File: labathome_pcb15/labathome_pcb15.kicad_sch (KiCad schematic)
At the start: 40 parts, among them J11 USB_ESP32, J15 CAN RS 485, J17 Micro_SD_Card_Det1, J21 GPIO, J22 Volts, J6 I2C, J7 PROG, SW2 YELLOW, SW3 GREEN, SW3 Reset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

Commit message: Updates in PCB, arduino test firmware
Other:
- note added: "Display (ST7789, 1,3'')"
- note added: "I2C addresses (0-127): AHT20: 0x38 BH1750 0x23 BMPx80: 0x76 CCS811: 0x5A LSM6DS3: 0x6A NAU88C22: 0x1A SCD41: 0x62 TCS34725: 0x29"
- note removed: "Display"
- note removed: "I2C addresses (0-127): AHT20: 0x38 BH1750 0x23 BMPx80: 0x76 CCS811: 0x5A LSM6DS3: 0x6A NAU88C22: 0x1A SCD41 0x62 TCS34725 0x29"
- company: (none) -> Klaus Liebler
- title: (none) -> lab@home
- moved on the sheet: C53, R39, R40, R41, SW3, SW4

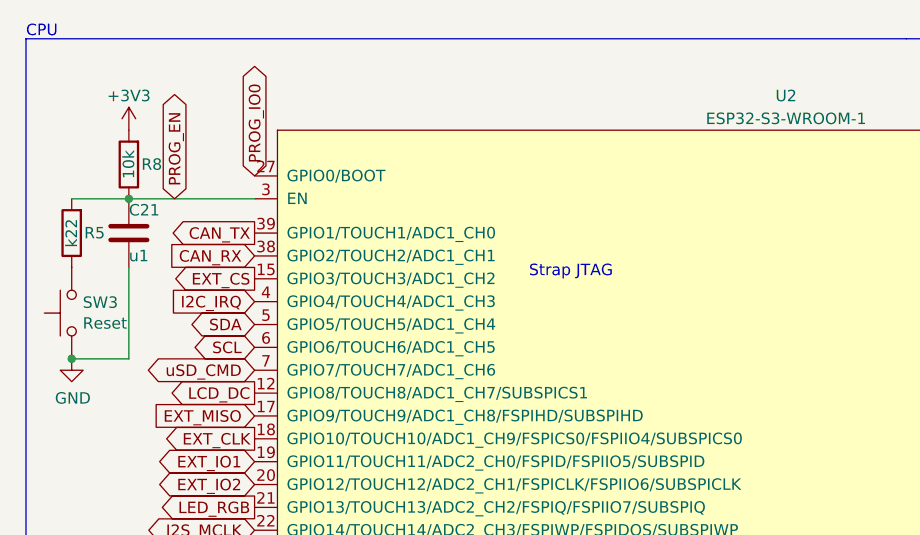
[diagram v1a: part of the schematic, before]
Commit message: Reverse mount LEDs, switch
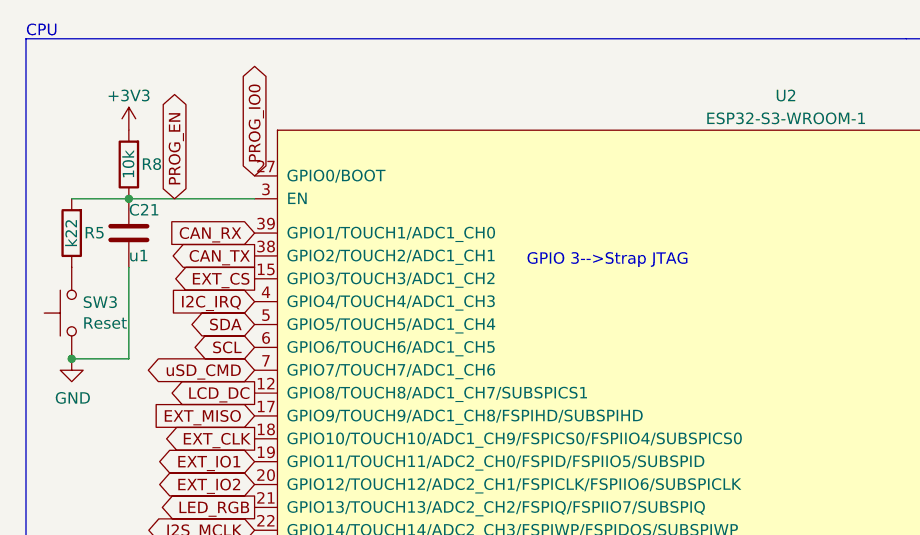
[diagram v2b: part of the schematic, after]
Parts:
- SW3: footprint liebler_MECH:SW_SPST_TL3342_smaller_handsolder -> liebler_MECH:Button_2x4x3,5_handsolder
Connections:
- net CAN_RX: now also U2.39 (GPIO1/TOUCH1/ADC1_CH0); no longer U2.38 (GPIO2/TOUCH2/ADC1_CH1)
- net CAN_TX: now also U2.38 (GPIO2/TOUCH2/ADC1_CH1); no longer U2.39 (GPIO1/TOUCH1/ADC1_CH0)
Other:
- note added: "GPIO 3-->Strap JTAG"
- note removed: "Strap JTAG"
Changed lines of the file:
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@@
 		)
 	)
-	(text "Strap JTAG"
+	(text "GPIO 3-->Strap JTAG"
 		(exclude_from_sim no)
-		(at 68.58 40.64 0)
+		(at 68.326 39.37 0)
 		(effects
 			(font
@@
 	(global_label "CAN_TX"
 		(shape output)
-		(at 38.1 35.56 180)
-		(fields_autoplaced yes)
-		(effects
-			(font
-				(size 1.27 1.27)
-			)
-			(justify right)
-		)
-		(property "Intersheetrefs" "${INTERSHEET_REFS}"
-			(at 28.281 35.56 0)
+		(at 38.1 38.1 180)
+		(fields_autoplaced yes)
+		(effects
+			(font
+				(size 1.27 1.27)
+			)
+			(justify right)
+		)
+		(property "Intersheetrefs" "${INTERSHEET_REFS}"
+			(at 28.281 38.1 0)
 			(effects
 				(font
@@
 	(global_label "CAN_RX"
 		(shape input)
-		(at 38.1 38.1 180)
-		(fields_autoplaced yes)
-		(effects
-			(font
-				(size 1.27 1.27)
-			)
-			(justify right)
-		)
-		(property "Intersheetrefs" "${INTERSHEET_REFS}"
-			(at 27.9786 38.1 0)
+		(at 38.1 35.56 180)
+		(fields_autoplaced yes)
+		(effects
+			(font
+				(size 1.27 1.27)
+			)
+			(justify right)
+		)
+		(property "Intersheetrefs" "${INTERSHEET_REFS}"
+			(at 27.9786 35.56 0)
 			(effects
 				(font
@@
 			)
 		)
-		(property "Footprint" "liebler_MECH:SW_SPST_TL3342_smaller_handsolder"
+		(property "Footprint" "liebler_MECH:Button_2x4x3,5_handsolder"
 			(at 12.7 44.45 0)
 			(effects

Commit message: Various last minute
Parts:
- C21, C26, C27, C32, C40, C53: footprint Capacitor_SMD:C_0402_1005Metric -> Capacitor_SMD:C_0201_0603Metric
- J7: value PROG -> PROG ESP
- R17, R44: value 1k -> 10k; footprint Resistor_SMD:R_0402_1005Metric -> Resistor_SMD:R_0201_0603Metric
- R39, R41, R56, R57, R58, R61, R62, R67, R8: footprint Resistor_SMD:R_0402_1005Metric -> Resistor_SMD:R_0201_0603Metric
- R40, R66: value 1k -> k22
- SW3, SW4: footprint Button_Switch_THT:SW_PUSH-12mm -> liebler_MECH:SW_Push_1P1T_NO_6x6mm_H6.5mm_Reverse
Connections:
- net GND: no longer SW2.MP
- new net GNDA: SW2.MP
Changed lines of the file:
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@@
 	)
 	(junction
-		(at 101.6 123.19)
-		(diameter 0)
-		(color 0 0 0 0)
-	)
-	(junction
 		(at 16.51 82.55)
 		(diameter 0)
@@
 	)
 	(junction
-		(at 203.2 38.1)
+		(at 101.6 123.19)
 		(diameter 0)
 		(color 0 0 0 0)
 	)
 	(junction
-		(at 208.28 41.91)
+		(at 203.2 38.1)
 		(diameter 0)
 		(color 0 0 0 0)
 	)
 	(junction
-		(at 142.24 105.41)
+		(at 208.28 41.91)
 		(diameter 0)
 		(color 0 0 0 0)
 	)
 	(junction
-		(at 100.33 123.19)
+		(at 142.24 105.41)
 		(diameter 0)
 		(color 0 0 0 0)
@@
 		)
 	)
-	(wire
-		(pts
-			(xy 92.71 123.19) (xy 100.33 123.19)
-		)
-		(stroke
-			(width 0)
-			(type default)
-		)
-	)
 	(polyline
 		(pts
@@
 		)
 	)
-	(wire
-		(pts
-			(xy 100.33 123.19) (xy 101.6 123.19)
-		)
-		(stroke
-			(width 0)
-			(type default)
-		)
-	)
 	(rectangle
 		(start 176.53 77.47)
@@
 	)
 	(symbol
+		(lib_id "power:GNDA")
+		(at 92.71 123.19 0)
+		(unit 1)
+		(exclude_from_sim no)
+		(in_bom yes)
+		(on_board yes)
+		(dnp no)
+		(fields_autoplaced yes)
+		(property "Reference" "#PWR0125"
+			(at 92.71 129.54 0)
+			(effects
+				(font
+					(size 1.27 1.27)
+				)
+				(hide yes)
+			)
+		)
+		(property "Value" "GNDA"
+			(at 92.71 128.27 0)
+			(effects
+				(font
+					(size 1.27 1.27)
+				)
+			)
+		)
+		(property "Footprint" ""
+			(at 92.71 123.19 0)
+			(effects
+				(font
+					(size 1.27 1.27)
+				)
+				(hide yes)
+			)
+		)
+		(property "Datasheet" ""
+			(at 92.71 123.19 0)
+			(effects
+				(font
+					(size 1.27 1.27)
+				)
+				(hide yes)
+			)
+		)
+		(property "Description" "Power symbol creates a global label with name \"GNDA\" , analog ground"
+			(at 92.71 123.19 0)
+			(effects
+				(font
+					(size 1.27 1.27)
+				)
+				(hide yes)
+			)
+		)
+		(pin "1"
+		)
+		(instances
+			(project "labathome_pcb15"
+				(path "/e4d6926a-1a8b-424d-97c4-66b6ad87e4ac"
+					(reference "#PWR0125")
+					(unit 1)
+				)
+			)
+		)
+	)
+	(symbol
 		(lib_id "power:GND")
 		(at 33.02 102.87 90)
@@
 			)
 		)
-		(property "Footprint" "Capacitor_SMD:C_0402_1005Metric"
+		(property "Footprint" "Capacitor_SMD:C_0201_0603Metric"
 			(at 150.1648 128.27 0)
 			(effects
@@
 			)
 		)
-		(property "Value" "PROG"
+		(property "Value" "PROG ESP"
 			(at 195.58 81.8896 0)
 			(effects
@@
 			)
 		)
-		(property "Footprint" "Resistor_SMD:R_0402_1005Metric"
+		(property "Footprint" "Resistor_SMD:R_0201_0603Metric"
 			(at 17.272 114.3 90)
 			(effects
@@
 			)
 		)
-		(property "Footprint" "Resistor_SMD:R_0402_1005Metric"
+		(property "Footprint" "Resistor_SMD:R_0201_0603Metric"
 			(at 154.432 109.22 90)
 			(effects
@@
 			)
 		)
-		(property "Value" "1k"
+		(property "Value" "10k"
 			(at 85.09 121.92 90)
 			(effects
@@
 			)
 		)
-		(property "Footprint" "Resistor_SMD:R_0402_1005Metric"
+		(property "Footprint" "Resistor_SMD:R_0201_0603Metric"
 			(at 86.868 121.92 90)
 			(effects
@@
 			)
 		)
-		(property "Footprint" "Resistor_SMD:R_0402_1005Metric"
+		(property "Footprint" "Resistor_SMD:R_0201_0603Metric"
 			(at 109.982 144.78 90)
 			(effects
@@
 	)
 	(symbol
-		(lib_id "power:GND")
-		(at 100.33 123.19 0)
-		(unit 1)
-		(exclude_from_sim no)
-		(in_bom yes)
-		(on_board yes)
-		(dnp no)
-		(property "Reference" "#PWR0125"
-			(at 100.33 129.54 0)
-			(effects
-				(font
-					(size 1.27 1.27)
-				)
-				(hide yes)
-			)
-		)
-		(property "Value" "GND"
-			(at 104.394 125.73 0)
-			(effects
-				(font
-					(size 1.27 1.27)
-				)
-			)
-		)
-		(property "Footprint" ""
-			(at 100.33 123.19 0)
-			(effects
-				(font
-					(size 1.27 1.27)
-				)
-				(hide yes)
-			)
-		)
-		(property "Datasheet" ""
-			(at 100.33 123.19 0)
-			(effects
-				(font
-					(size 1.27 1.27)
-				)
-				(hide yes)
-			)
-		)
-		(property "Description" "Power symbol creates a global label with name \"GND\" , ground"
-			(at 100.33 123.19 0)
-			(effects
-				(font
-					(size 1.27 1.27)
-				)
-				(hide yes)
-			)
-		)
-		(pin "1"
-		)
-		(instances
-			(project "labathome_pcb15"
-				(path "/e4d6926a-1a8b-424d-97c4-66b6ad87e4ac"
-					(reference "#PWR0125")
-					(unit 1)
-				)
-			)
-		)
-	)
-	(symbol
 		(lib_id "Device:C")
 		(at 110.49 116.84 180)
@@
 			)
 		)
-		(property "Footprint" "Capacitor_SMD:C_0402_1005Metric"
+		(property "Footprint" "Capacitor_SMD:C_0201_0603Metric"
 			(at 109.5248 113.03 0)
 			(effects
@@
 			)
 		)
-		(property "Footprint" "Capacitor_SMD:C_0402_1005Metric"
+		(property "Footprint" "Capacitor_SMD:C_0201_0603Metric"
 			(at 17.4752 90.17 0)
 			(effects
@@
 			)
 		)
-		(property "Footprint" "Resistor_SMD:R_0402_1005Metric"
+		(property "Footprint" "Resistor_SMD:R_0201_0603Metric"
 			(at 140.462 116.84 90)
 			(effects
@@
 			)
 		)
-		(property "Value" "1k"
+		(property "Value" "k22"
 			(at 105.41 148.59 90)
 			(effects
@@
 			)
 		)
-		(property "Footprint" "Capacitor_SMD:C_0402_1005Metric"
+		(property "Footprint" "Capacitor_SMD:C_0201_0603Metric"
 			(at 110.7948 148.59 0)
 			(effects
@@
 			)
 		)
-		(property "Footprint" "Resistor_SMD:R_0402_1005Metric"
+		(property "Footprint" "Resistor_SMD:R_0201_0603Metric"
 			(at 134.112 121.92 90)
 			(effects
@@
 	)
 	(symbol
+		(lib_id "power:GND")
+		(at 101.6 123.19 0)
+		(unit 1)
+		(exclude_from_sim no)
+		(in_bom yes)
+		(on_board yes)
+		(dnp no)
+		(property "Reference" "#PWR0203"
+			(at 101.6 129.54 0)
+			(effects
+				(font
+					(size 1.27 1.27)
+				)
+				(hide yes)
+			)
+		)
+		(property "Value" "GND"
+			(at 101.6 128.27 90)
+			(effects
+				(font
+					(size 1.27 1.27)
+				)
+			)
+		)
+		(property "Footprint" ""
+			(at 101.6 123.19 0)
+			(effects
+				(font
+					(size 1.27 1.27)
+				)
+				(hide yes)
+			)
+		)
+		(property "Datasheet" ""
+			(at 101.6 123.19 0)
+			(effects
+				(font
+					(size 1.27 1.27)
+				)
+				(hide yes)
+			)
+		)
+		(property "Description" "Power symbol creates a global label with name \"GND\" , ground"
+			(at 101.6 123.19 0)
+			(effects
+				(font
+					(size 1.27 1.27)
+				)
+				(hide yes)
+			)
+		)
+		(pin "1"
+		)
+		(instances
+			(project "labathome_pcb15"
+				(path "/e4d6926a-1a8b-424d-97c4-66b6ad87e4ac"
+					(reference "#PWR0203")
+					(unit 1)
+				)
+			)
+		)
+	)
+	(symbol
 		(lib_id "Device:C")
 		(at 22.86 106.68 180)
@@
 			)
 		)
-		(property "Footprint" "Capacitor_SMD:C_0402_1005Metric"
+		(property "Footprint" "Capacitor_SMD:C_0201_0603Metric"
 			(at 21.8948 102.87 0)
 			(effects
@@
 			)
 		)
-		(property "Footprint" "Resistor_SMD:R_0402_1005Metric"
+		(property "Footprint" "Resistor_SMD:R_0201_0603Metric"
 			(at 79.502 148.59 90)
 			(effects
@@
 			)
 		)
-		(property "Footprint" "Resistor_SMD:R_0402_1005Metric"
+		(property "Footprint" "Resistor_SMD:R_0201_0603Metric"
 			(at 149.352 111.76 90)
 			(effects
@@
 			)
 		)
-		(property "Footprint" "Button_Switch_THT:SW_PUSH-12mm"
+		(property "Footprint" "liebler_MECH:SW_Push_1P1T_NO_6x6mm_H6.5mm_Reverse"
 			(at 96.52 153.67 0)
 			(effects
@@
 			)
 		)
-		(property "Value" "1k"
+		(property "Value" "k22"
 			(at 105.41 113.03 90)
 			(effects
@@
 			)
 		)
-		(property "Footprint" "Resistor_SMD:R_0402_1005Metric"
+		(property "Footprint" "Resistor_SMD:R_0201_0603Metric"
 			(at 25.908 27.94 90)
 			(effects
@@
 			)
 		)
-		(property "Footprint" "Button_Switch_THT:SW_PUSH-12mm"
+		(property "Footprint" "liebler_MECH:SW_Push_1P1T_NO_6x6mm_H6.5mm_Reverse"
 			(at 76.2 139.7 0)
 			(effects
@@
 			)
 		)
-		(property "Footprint" "Capacitor_SMD:C_0402_1005Metric"
+		(property "Footprint" "Capacitor_SMD:C_0201_0603Metric"
 			(at 25.0952 39.37 0)
 			(effects
@@
 			)
 		)
-		(property "Footprint" "Resistor_SMD:R_0402_1005Metric"
+		(property "Footprint" "Resistor_SMD:R_0201_0603Metric"
 			(at 108.712 109.22 90)
 			(effects
@@
 			)
 		)
-		(property "Value" "1k"
+		(property "Value" "10k"
 			(at 85.09 109.22 90)
 			(effects
@@
 			)
 		)
-		(property "Footprint" "Resistor_SMD:R_0402_1005Metric"
+		(property "Footprint" "Resistor_SMD:R_0201_0603Metric"
 			(at 86.868 109.22 90)
 			(effects

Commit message: PCB update IP5306 I2C
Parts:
- J7: footprint liebler_CONN:IDC_2x03_P1.27mm_Vertical -> liebler_CONN:PinHeader_2x03_P1.27mm_Vertical_SMD_handsolder
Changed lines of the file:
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@@
 			)
 		)
-		(property "Footprint" "liebler_CONN:IDC_2x03_P1.27mm_Vertical"
+		(property "Footprint" "liebler_CONN:PinHeader_2x03_P1.27mm_Vertical_SMD_handsolder"
 			(at 194.31 87.63 0)
 			(effects

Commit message: 4 Layers
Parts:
- R10, R9: footprint Resistor_SMD:R_0402_1005Metric -> Resistor_SMD:R_0201_0603Metric
- R5, R8: value 4k7 -> 3k3
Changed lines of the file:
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@@
 			)
 		)
-		(property "Value" "4k7"
+		(property "Value" "3k3"
 			(at 68.58 106.68 90)
 			(effects
@@
 			)
 		)
-		(property "Footprint" "Resistor_SMD:R_0402_1005Metric"
+		(property "Footprint" "Resistor_SMD:R_0201_0603Metric"
 			(at 207.01 29.718 90)
 			(effects
@@
 			)
 		)
-		(property "Footprint" "Resistor_SMD:R_0402_1005Metric"
+		(property "Footprint" "Resistor_SMD:R_0201_0603Metric"
 			(at 207.01 32.258 90)
 			(effects
@@
 			)
 		)
-		(property "Value" "4k7"
+		(property "Value" "3k3"
 			(at 63.5 106.68 90)
 			(effects

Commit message: Various changes / bugfixes / refactorings
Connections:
- net LCD_RES: now reaches R62.2, U21.5 (RES)
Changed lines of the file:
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@@
+		)
+	)
+	(global_label "LCD_RES"
+		(shape input)
+		(at 19.05 118.11 180)
+		(fields_autoplaced yes)
+		(effects
+			(font
+				(size 1.27 1.27)
+			)
+			(justify right)
+		)
+		(property "Intersheetrefs" "${INTERSHEET_REFS}"
+			(at 7.9006 118.11 0)
+			(effects
+				(font
+					(size 1.27 1.27)
+				)
+				(justify right)
+				(hide yes)
+			)
 		)
 	)

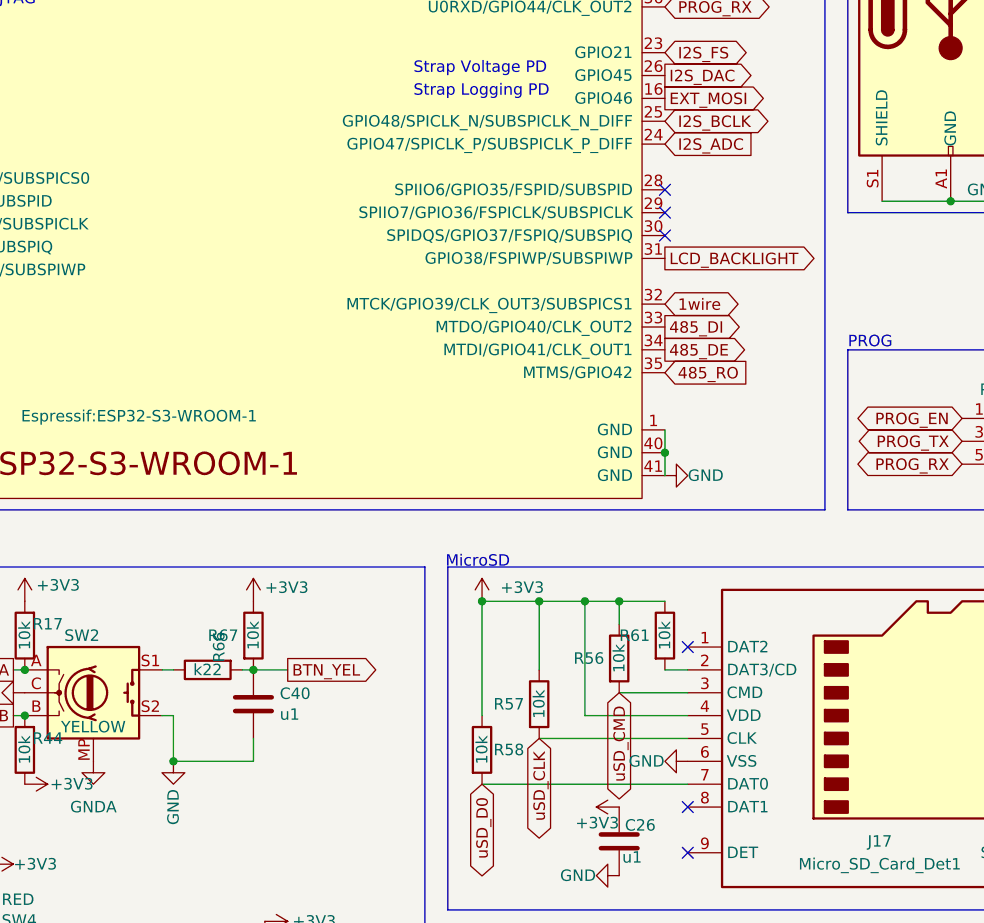
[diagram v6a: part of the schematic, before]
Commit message: ec11 smd, LCD Reset from ESP32 with jumper, six servos
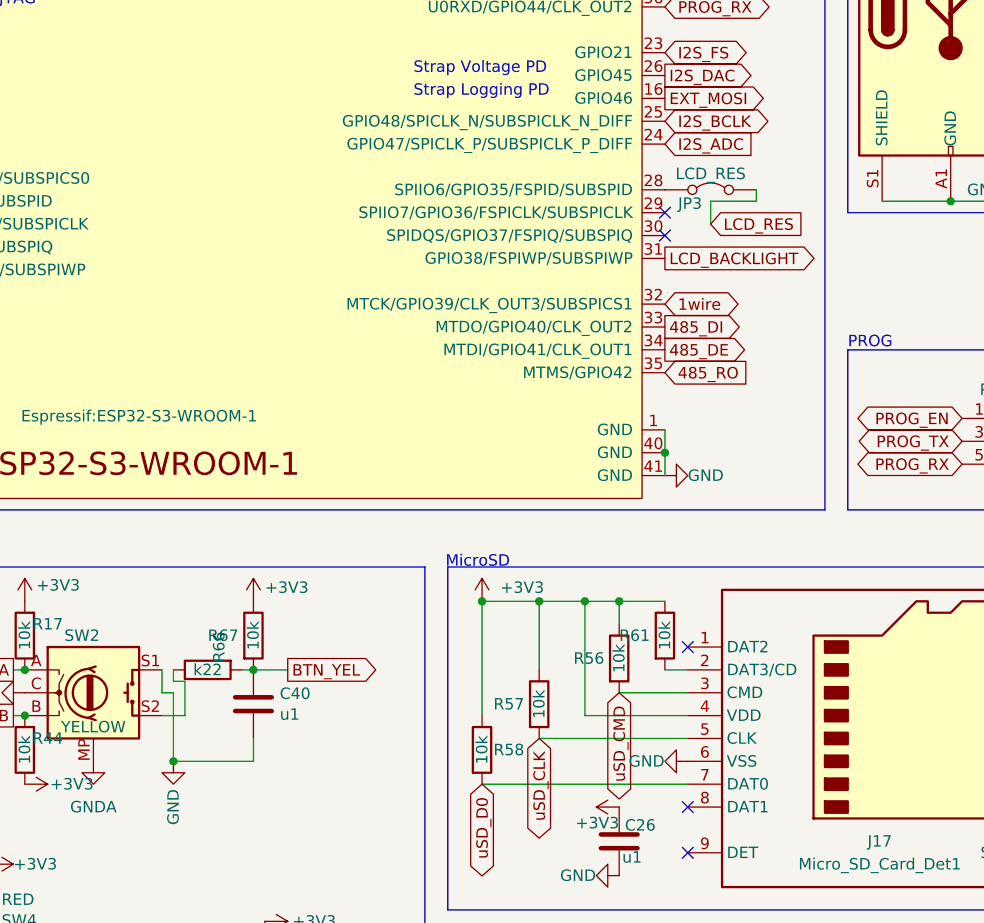
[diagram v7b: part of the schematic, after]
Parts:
- added JP3: LCD_RES, Jumper:SolderJumper-2_P1.3mm_Bridged2Bar_RoundedPad1.0x1.5mm, symbol Jumper:Jumper_2_Bridged
- SW2: footprint liebler_MECH:RotaryEncoder_Alps_EC11E-Switch_Vertical_H20mm -> liebler_MECH:RotaryEncoder_EC11_SMD_handsolder
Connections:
- net GND: now also SW2.S1; no longer SW2.S2
- net LCD_RES: now also JP3.2 (B)
- net at U2.28 (SPIIO6/GPIO35/FSPID/SUBSPID): now also JP3.1 (A)
- net at R66.1: now also SW2.S2; no longer SW2.S1
- no-connect marks 8 -> 7
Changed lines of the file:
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@@
 	)
 	(no_connect
-		(at 156.21 59.69)
-	)
-	(no_connect
 		(at 156.21 64.77)
 	)
@@
 	(wire
 		(pts
+			(xy 161.29 60.96) (xy 161.29 63.5)
+		)
+		(stroke
+			(width 0)
+			(type default)
+		)
+	)
+	(wire
+		(pts
 			(xy 31.75 102.87) (xy 33.02 102.87)
 		)
@@
 	(wire
 		(pts
-			(xy 101.6 118.11) (xy 100.33 118.11)
+			(xy 101.6 113.03) (xy 101.6 114.3)
 		)
 		(stroke
@@
 	(wire
 		(pts
-			(xy 22.86 110.49) (xy 27.94 110.49)
+			(xy 101.6 115.57) (xy 101.6 123.19)
 		)
 		(stroke
@@
 	(wire
 		(pts
-			(xy 85.09 118.11) (xy 83.82 118.11)
+			(xy 22.86 110.49) (xy 27.94 110.49)
 		)
 		(stroke
@@
 	(wire
 		(pts
-			(xy 100.33 113.03) (xy 101.6 113.03)
+			(xy 85.09 118.11) (xy 83.82 118.11)
 		)
 		(stroke
@@
 	(wire
 		(pts
+			(xy 166.37 60.96) (xy 161.29 60.96)
+		)
+		(stroke
+			(width 0)
+			(type default)
+		)
+	)
+	(wire
+		(pts
+			(xy 102.87 118.11) (xy 102.87 114.3)
+		)
+		(stroke
+			(width 0)
+			(type default)
+		)
+	)
+	(wire
+		(pts
 			(xy 24.13 39.37) (xy 24.13 49.53)
 		)
@@
 		)
 	)
+	(wire
+		(pts
+			(xy 100.33 118.11) (xy 102.87 118.11)
+		)
+		(stroke
+			(width 0)
+			(type default)
+		)
+	)
 	(polyline
 		(pts
@@
 	(wire
 		(pts
-			(xy 24.13 49.53) (xy 17.78 49.53)
+			(xy 100.33 115.57) (xy 100.33 113.03)
 		)
 		(stroke
@@
 	(wire
 		(pts
-			(xy 110.49 120.65) (xy 110.49 123.19)
+			(xy 166.37 59.69) (xy 166.37 60.96)
 		)
 		(stroke
@@
 	(wire
 		(pts
-			(xy 101.6 118.11) (xy 101.6 123.19)
+			(xy 24.13 49.53) (xy 17.78 49.53)
+		)
+		(stroke
+			(width 0)
+			(type default)
+		)
+	)
+	(wire
+		(pts
+			(xy 110.49 120.65) (xy 110.49 123.19)
 		)
 		(stroke
@@
 	(wire
 		(pts
+			(xy 102.87 114.3) (xy 101.6 114.3)
+		)
+		(stroke
+			(width 0)
+			(type default)
+		)
+	)
+	(wire
+		(pts
 			(xy 210.82 27.94) (xy 212.09 27.94)
 		)
@@
 	(wire
 		(pts
+			(xy 101.6 115.57) (xy 100.33 115.57)
+		)
+		(stroke
+			(width 0)
+			(type default)
+		)
+	)
+	(wire
+		(pts
 			(xy 115.57 146.05) (xy 115.57 148.59)
 		)
@@
 		)
 	)
+	(global_label "LCD_RES"
+		(shape input)
+		(at 161.29 63.5 0)
+		(fields_autoplaced yes)
+		(effects
+			(font
+				(size 1.27 1.27)
+			)
+			(justify left)
+		)
+		(property "Intersheetrefs" "${INTERSHEET_REFS}"
+			(at 172.4394 63.5 0)
+			(effects
+				(font
+					(size 1.27 1.27)
+				)
+				(justify left)
+				(hide yes)
+			)
+		)
+	)
 	(global_label "EXT_MISO"
 		(shape input)
@@
 	)
 	(symbol
+		(lib_id "Jumper:Jumper_2_Bridged")
+		(at 161.29 59.69 0)
+		(unit 1)
+		(exclude_from_sim yes)
+		(in_bom yes)
+		(on_board yes)
+		(dnp no)
+		(property "Reference" "JP3"
+			(at 159.004 61.214 0)
+			(effects
+				(font
+					(size 1.27 1.27)
+				)
+			)
+		)
+		(property "Value" "LCD_RES"
+			(at 161.29 57.912 0)
+			(effects
+				(font
+					(size 1.27 1.27)
+				)
+			)
+		)
+		(property "Footprint" "Jumper:SolderJumper-2_P1.3mm_Bridged2Bar_RoundedPad1.0x1.5mm"
+			(at 161.29 59.69 0)
+			(effects
+				(font
+					(size 1.27 1.27)
+				)
+				(hide yes)
+			)
+		)
+		(property "Datasheet" "~"
+			(at 161.29 59.69 0)
+			(effects
+				(font
+					(size 1.27 1.27)
+				)
+				(hide yes)
+			)
+		)
+		(property "Description" "Jumper, 2-pole, closed/bridged"
+			(at 161.29 59.69 0)
+			(effects
+				(font
+					(size 1.27 1.27)
+				)
+				(hide yes)
+			)
+		)
+		(pin "1"
+		)
+		(pin "2"
+		)
+		(instances
+			(project ""
+				(path "/e4d6926a-1a8b-424d-97c4-66b6ad87e4ac"
+					(reference "JP3")
+					(unit 1)
+				)
+			)
+		)
+	)
+	(symbol
 		(lib_id "Device:R")
 		(at 58.42 106.68 180)
@@
 			)
 		)
-		(property "Footprint" "liebler_MECH:RotaryEncoder_Alps_EC11E-Switch_Vertical_H20mm"
+		(property "Footprint" "liebler_MECH:RotaryEncoder_EC11_SMD_handsolder"
 			(at 88.9 111.506 0)
 			(effects
